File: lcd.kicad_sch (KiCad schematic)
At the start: 0 parts

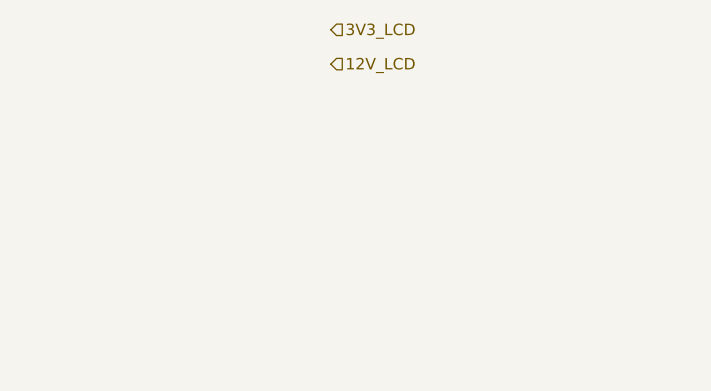
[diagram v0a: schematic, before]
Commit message: Add RGB 24 bits bus
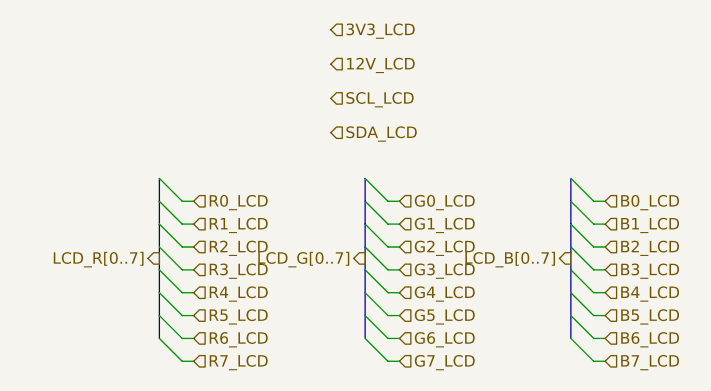
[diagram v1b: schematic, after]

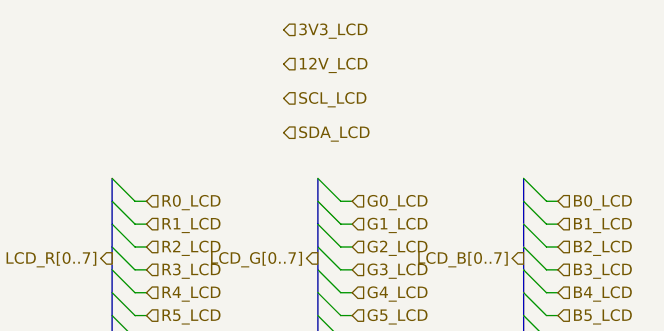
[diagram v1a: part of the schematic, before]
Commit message: Add WLED driver in power shcematic
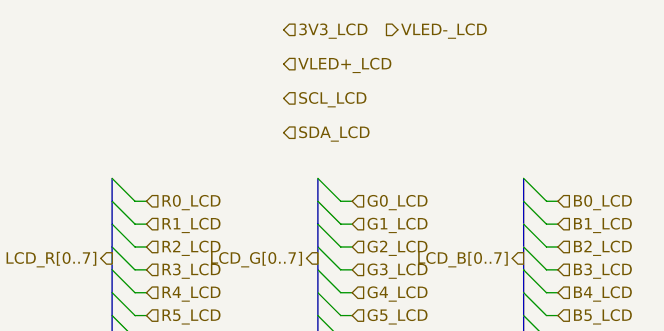
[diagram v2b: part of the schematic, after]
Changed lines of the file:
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@@
-		)
-	)
-	(hierarchical_label "12V_LCD"
-		(shape input)
-		(at 128.27 83.82 0)
-		(effects
-			(font
-				(size 1.27 1.27)
-			)
-			(justify left)
 		)
 	)
@@
 		(shape input)
 		(at 135.89 99.06 0)
+		(effects
+			(font
+				(size 1.27 1.27)
+			)
+			(justify left)
+		)
+	)
+	(hierarchical_label "VLED+_LCD"
+		(shape input)
+		(at 128.27 83.82 0)
 		(effects
 			(font
@@
 		(effects
 			(font
+				(size 1.27 1.27)
+			)
+			(justify left)
+		)
+	)
+	(hierarchical_label "VLED-_LCD"
+		(shape output)
+		(at 139.7 80.01 0)
+		(effects
+			(font

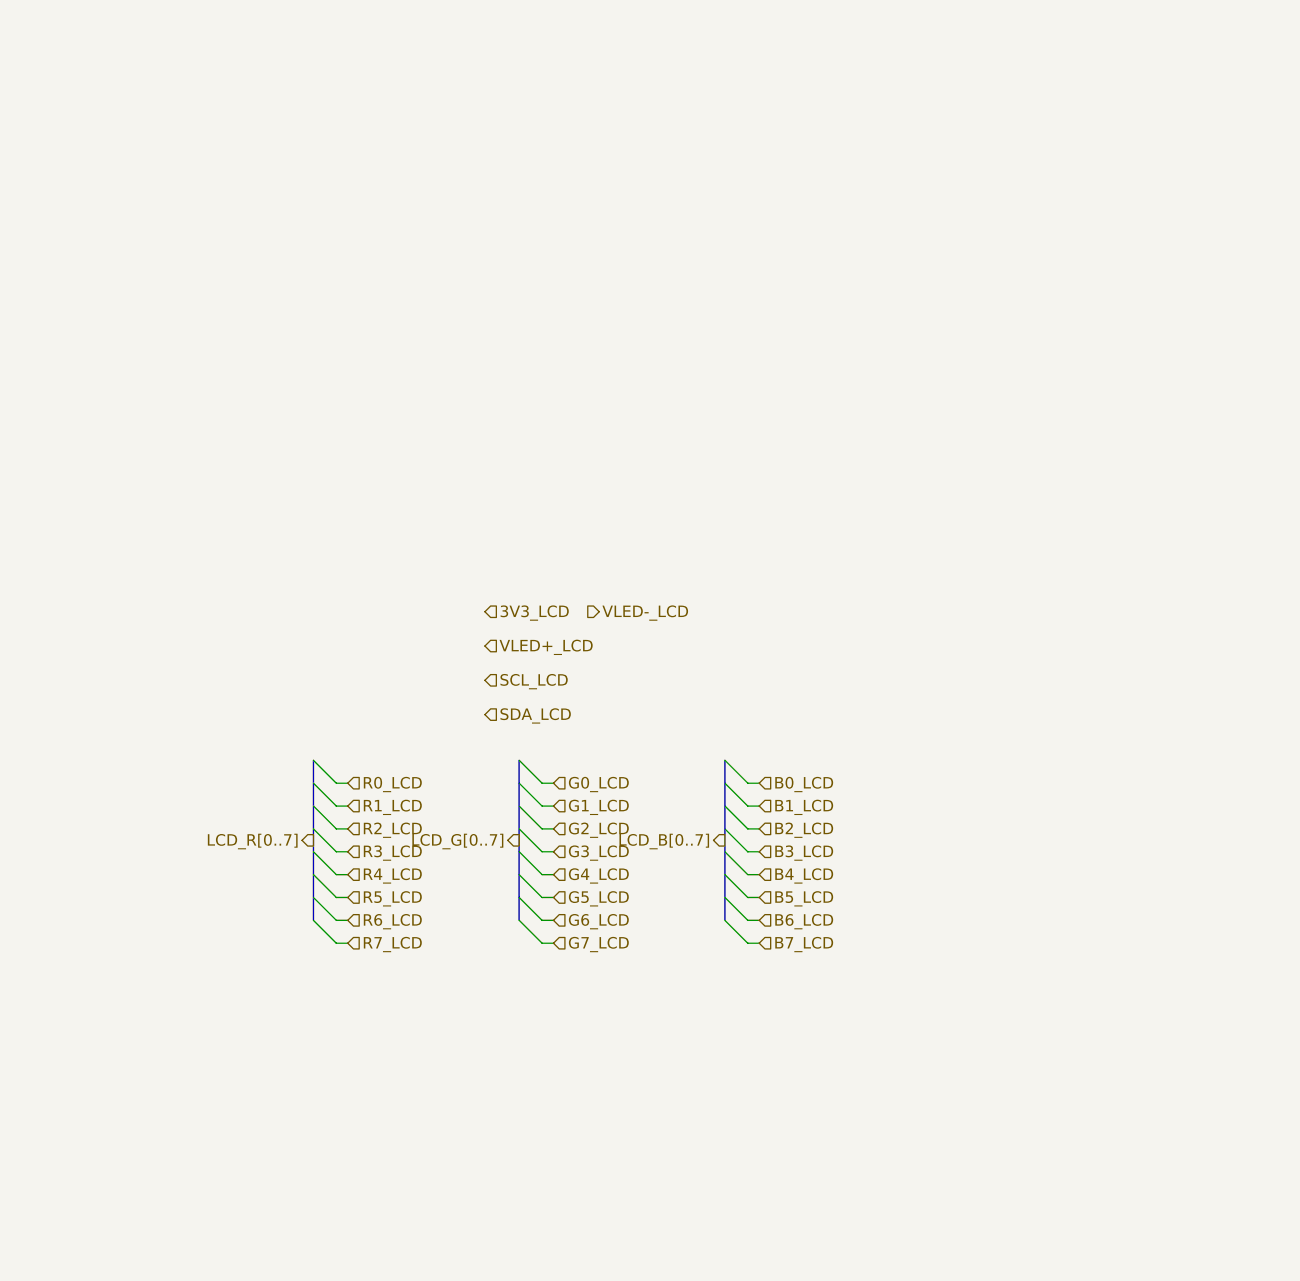
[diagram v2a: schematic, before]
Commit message: Add FPC/FFC connectors for LCD display screen
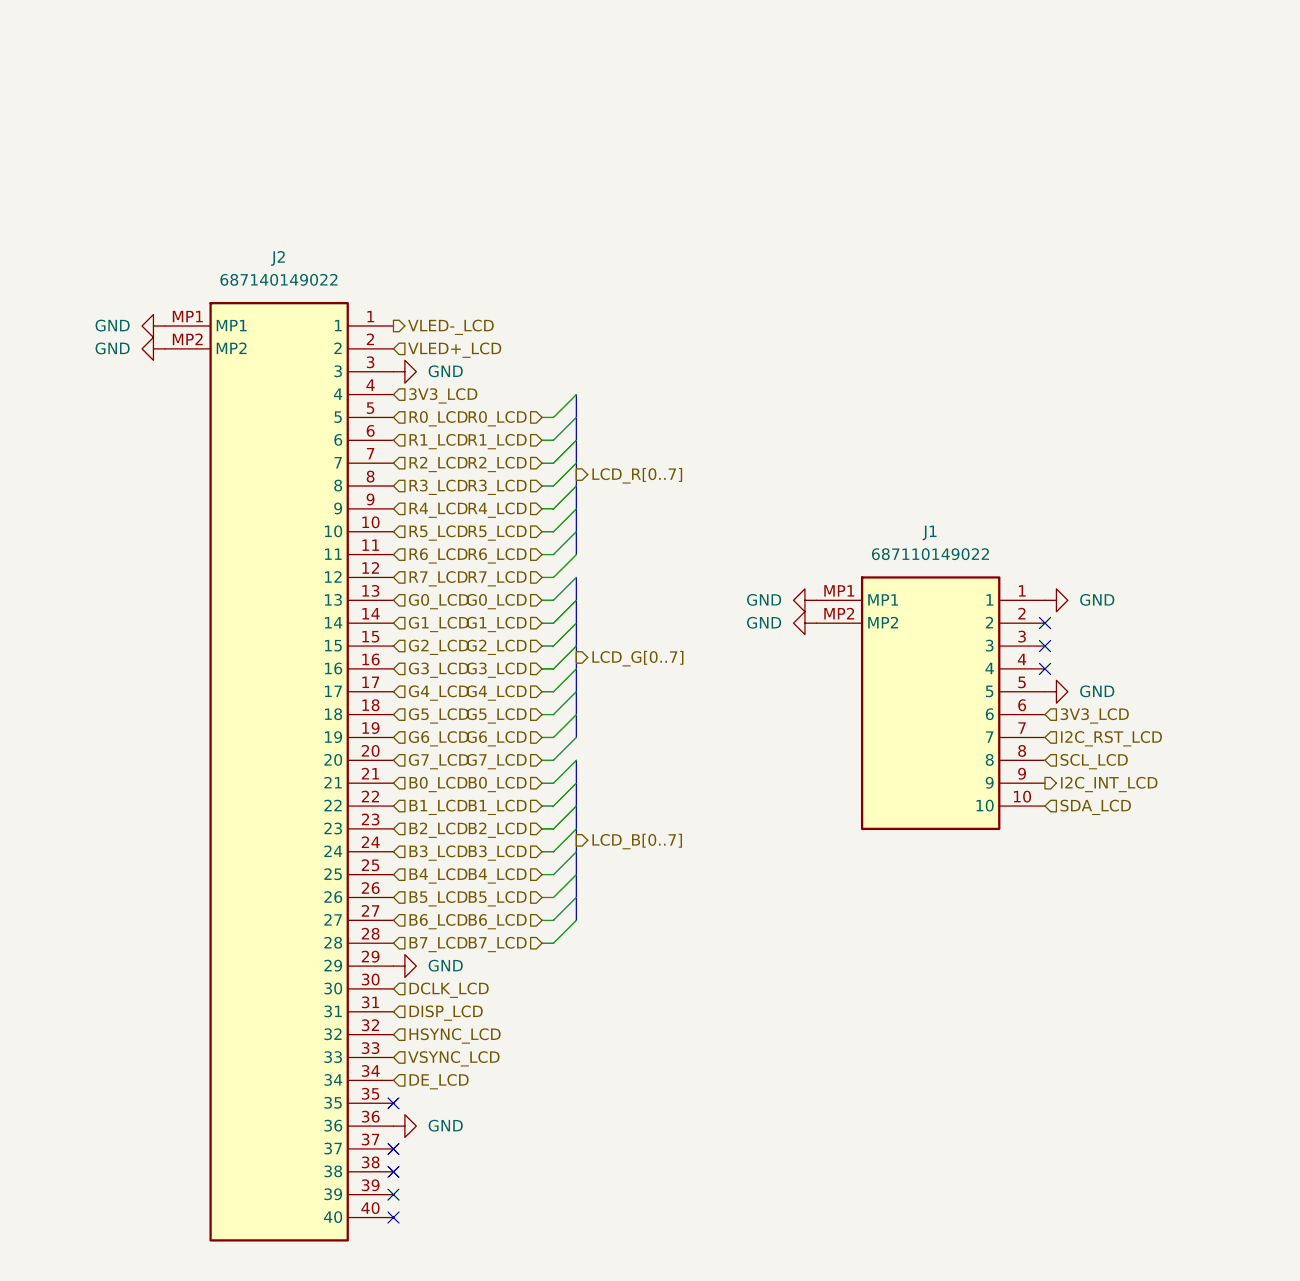
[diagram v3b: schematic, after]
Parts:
- added J1: 687110149022, 687110149022, symbol weather-station-poc-sym:687110149022
- added J2: 687140149022, 687140149022, symbol weather-station-poc-sym:687140149022
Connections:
- net 3V3_LCD: now also J1.6, J2.4
- net B0_LCD: now also J2.21
- net B1_LCD: now also J2.22
- net B2_LCD: now also J2.23
- net B3_LCD: now also J2.24
- net B4_LCD: now also J2.25
- net B5_LCD: now also J2.26
- net B6_LCD: now also J2.27
- net B7_LCD: now also J2.28
- net G0_LCD: now also J2.13
- net G1_LCD: now also J2.14
- net G2_LCD: now also J2.15
- net G3_LCD: now also J2.16
- net G4_LCD: now also J2.17
- net G5_LCD: now also J2.18
- net G6_LCD: now also J2.19
- net G7_LCD: now also J2.20
- net R0_LCD: now also J2.5
- net R1_LCD: now also J2.6
- net R2_LCD: now also J2.7
- net R3_LCD: now also J2.8
- net R4_LCD: now also J2.9
- net R5_LCD: now also J2.10
- net R6_LCD: now also J2.11
- net R7_LCD: now also J2.12
- net SCL_LCD: now also J1.8
- net SDA_LCD: now also J1.10
- net VLED+_LCD: now also J2.2
- net VLED-_LCD: now also J2.1
- new net DCLK_LCD: J2.30
- new net DE_LCD: J2.34
- new net DISP_LCD: J2.31
- new net GND: J1.1, J1.5, J1.MP1, J1.MP2, J2.29, J2.3, J2.36, J2.MP1, J2.MP2
- new net HSYNC_LCD: J2.32
- new net I2C_INT_LCD: J1.9
- new net I2C_RST_LCD: J1.7
- new net VSYNC_LCD: J2.33
- no-connect marks 0 -> 8

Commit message: Use local labels for RGB bus in folio and add title for all folio
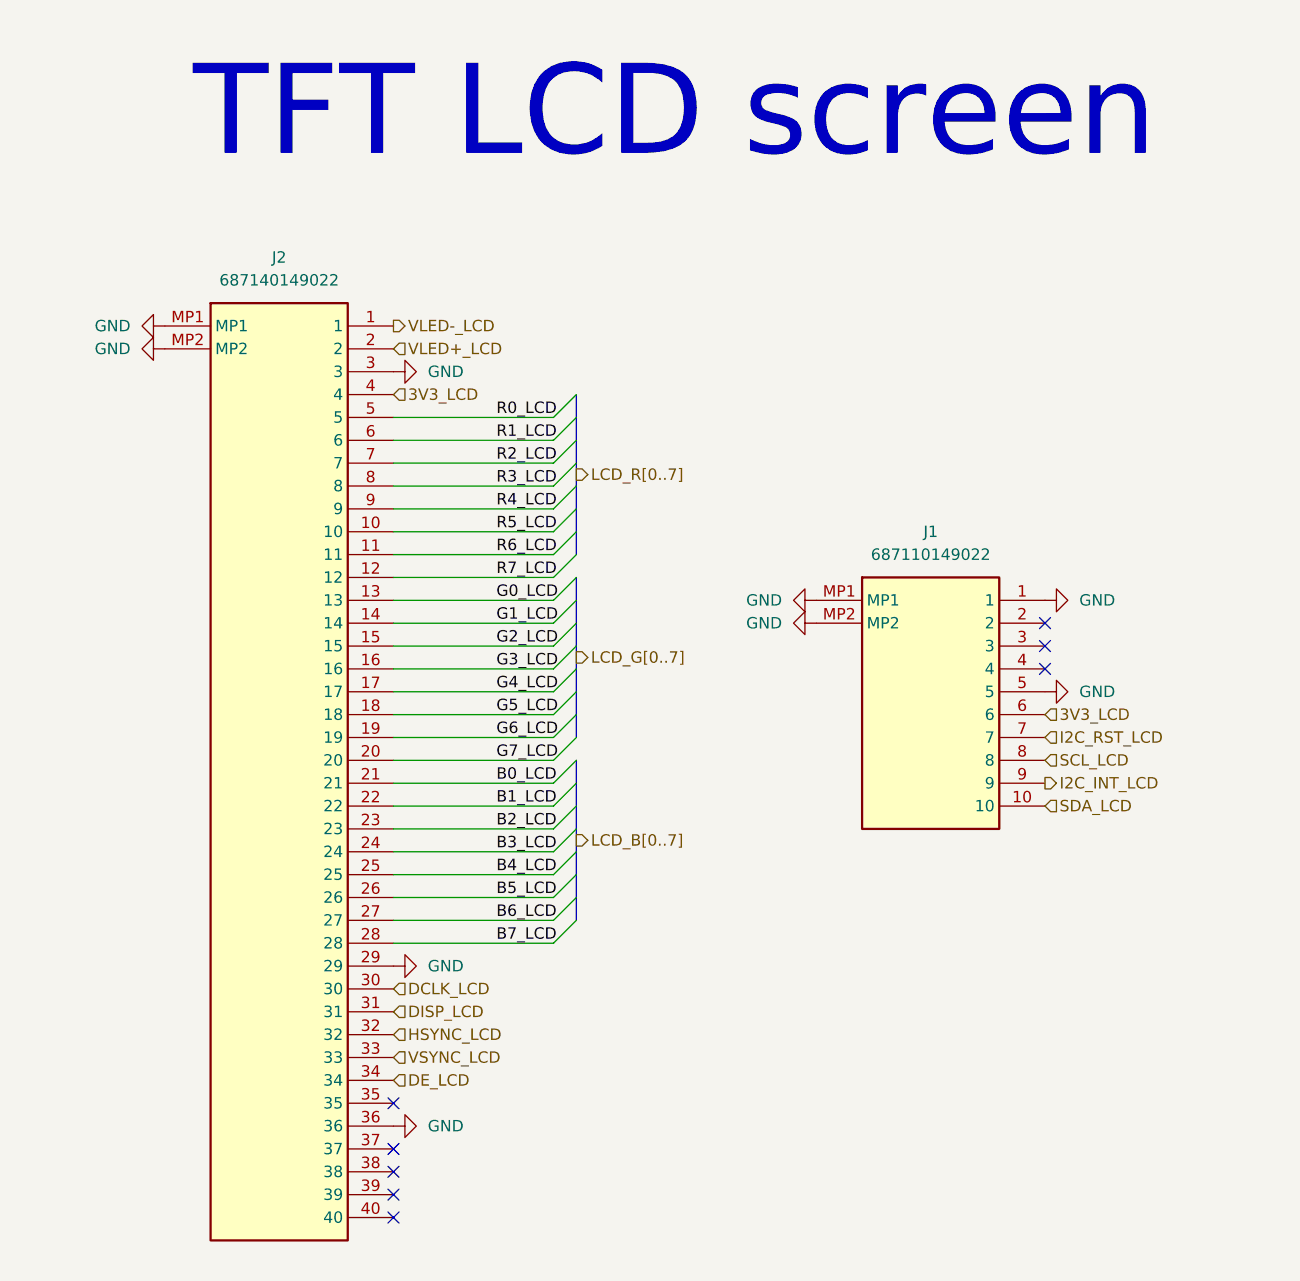
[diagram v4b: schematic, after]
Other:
- note added: "TFT LCD screen"
